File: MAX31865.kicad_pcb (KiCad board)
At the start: 2 copper layers, 25.4 x 27.9 mm, 29 parts, among them U1 MAX31865, U3 MIC5225-3.3, X1 3.5mm, X2 3.5mm

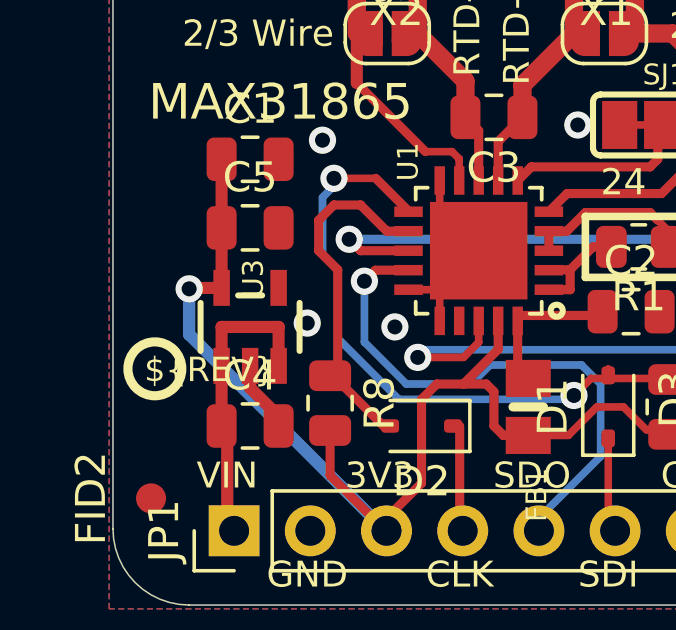
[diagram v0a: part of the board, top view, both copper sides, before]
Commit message: changed sot-23-5 footprint in schematic and pcb layout
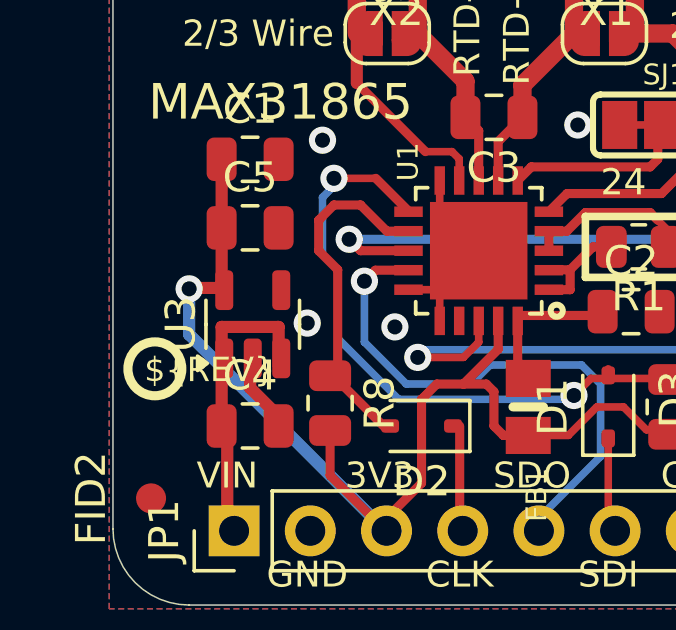
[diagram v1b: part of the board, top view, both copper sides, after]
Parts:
- U3: footprint SOT23-5 -> Package_TO_SOT_SMD:SOT-23-5
- moved U3 0.12 mm to (140.5, 109.6), turned to 90 degrees
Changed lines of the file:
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@@
 		)
 	)
-	(footprint "SOT23-5"
+	(footprint "Package_TO_SOT_SMD:SOT-23-5"
 		(layer "F.Cu")
-		(at 140.3731 109.7026)
-		(descr "Small Outline Transistor - 5 Pin")
+		(at 140.4606 109.6151 90)
+		(descr "SOT, 5 Pin (https://www.jedec.org/sites/default/files/docs/Mo-178c.PDF variant AA), generated with kicad-footprint-generator ipc_gullwing_generator.py")
+		(tags "SOT TO_SOT_SMD")
 		(property "Reference" "U3"
-			(at 0.508 -0.962 90)
+			(at 0 -2.4 270)
+			(layer "F.SilkS")
+			(effects
+				(font
+					(size 1 1)
+					(thickness 0.15)
+				)
+			)
+		)
+		(property "Value" "MIC5225-3.3"
+			(at 0 2.4 270)
+			(layer "F.Fab")
+			(effects
+				(font
+					(size 1 1)
+					(thickness 0.15)
+				)
+			)
+		)
+		(property "Footprint" ""
+			(at 0 0 90)
 			(unlocked yes)
-			(layer "F.SilkS")
-			(effects
-				(font
-					(size 0.692831 0.692831)
-					(thickness 0.119969)
-				)
-				(justify left bottom)
-			)
-		)
-		(property "Value" "MIC5225-3.3"
-			(at -4.899 -0.762 0)
+			(layer "F.Fab")
+			(hide yes)
+			(effects
+				(font
+					(size 1.27 1.27)
+				)
+			)
+		)
+		(property "Datasheet" ""
+			(at 0 0 90)
 			(unlocked yes)
 			(layer "F.Fab")
-			(effects
-				(font
-					(size 0.979424 0.979424)
-					(thickness 0.036576)
-				)
-				(justify right top)
-			)
-		)
-		(property "Footprint" ""
-			(at 0 0 0)
+			(hide yes)
+			(effects
+				(font
+					(size 1.27 1.27)
+				)
+			)
+		)
+		(property "Description" ""
+			(at 0 0 90)
 			(unlocked yes)
 			(layer "F.Fab")
@@
 			)
 		)
-		(property "Datasheet" ""
-			(at 0 0 0)
-			(unlocked yes)
-			(layer "F.Fab")
-			(hide yes)
-			(effects
-				(font
-					(size 1.27 1.27)
-				)
-			)
-		)
-		(property "Description" ""
-			(at 0 0 0)
-			(unlocked yes)
-			(layer "F.Fab")
-			(hide yes)
-			(effects
-				(font
-					(size 1.27 1.27)
-				)
-			)
-		)
-		(fp_line
-			(start -1.65 -0.8)
-			(end -1.65 0.8)
-			(stroke
-				(width 0.2032)
-				(type solid)
-			)
-			(layer "F.SilkS")
-		)
-		(fp_line
-			(start -0.4 -1.05)
-			(end 0.4 -1.05)
-			(stroke
-				(width 0.2032)
-				(type solid)
-			)
-			(layer "F.SilkS")
-		)
-		(fp_line
-			(start 1.65 -0.8)
-			(end 1.65 0.8)
-			(stroke
-				(width 0.2032)
-				(type solid)
-			)
-			(layer "F.SilkS")
-		)
-		(fp_line
-			(start -1.4224 -0.8104)
-			(end 1.4224 -0.8104)
-			(stroke
-				(width 0.2032)
-				(type solid)
-			)
-			(layer "F.Fab")
-		)
-		(fp_line
-			(start -1.4224 0.8104)
-			(end -1.4224 -0.8104)
-			(stroke
-				(width 0.2032)
-				(type solid)
-			)
-			(layer "F.Fab")
-		)
-		(fp_line
-			(start 1.4224 -0.8104)
-			(end 1.4224 0.8104)
-			(stroke
-				(width 0.2032)
-				(type solid)
-			)
-			(layer "F.Fab")
-		)
-		(fp_line
-			(start 1.4224 0.8104)
-			(end -1.4224 0.8104)
-			(stroke
-				(width 0.2032)
-				(type solid)
-			)
-			(layer "F.Fab")
+		(attr smd)
+		(fp_line
+			(start 0 -1.56)
+			(end 0.8 -1.56)
+			(stroke
+				(width 0.12)
+				(type solid)
+			)
+			(layer "F.SilkS")
+		)
+		(fp_line
+			(start 0 -1.56)
+			(end -0.8 -1.56)
+			(stroke
+				(width 0.12)
+				(type solid)
+			)
+			(layer "F.SilkS")
+		)
+		(fp_line
+			(start 0 1.56)
+			(end 0.8 1.56)
+			(stroke
+				(width 0.12)
+				(type solid)
+			)
+			(layer "F.SilkS")
+		)
+		(fp_line
+			(start 0 1.56)
+			(end -0.8 1.56)
+			(stroke
+				(width 0.12)
+				(type solid)
+			)
+			(layer "F.SilkS")
 		)
 		(fp_poly
 			(pts
-				(xy -1.2 -0.85) (xy -0.7 -0.85) (xy -0.7 -1.5) (xy -1.2 -1.5)
-			)
-			(stroke
-				(width 0)
-				(type default)
+				(xy -1.3 -1.51) (xy -1.54 -1.84) (xy -1.06 -1.84) (xy -1.3 -1.51)
+			)
+			(stroke
+				(width 0.12)
+				(type solid)
 			)
 			(fill solid)
-			(layer "F.Fab")
-		)
-		(fp_poly
-			(pts
-				(xy -1.2 1.5) (xy -0.7 1.5) (xy -0.7 0.85) (xy -1.2 0.85)
-			)
-			(stroke
-				(width 0)
-				(type default)
-			)
-			(fill solid)
-			(layer "F.Fab")
-		)
-		(fp_poly
-			(pts
-				(xy -0.25 1.5) (xy 0.25 1.5) (xy 0.25 0.85) (xy -0.25 0.85)
-			)
-			(stroke
-				(width 0)
-				(type default)
-			)
-			(fill solid)
-			(layer "F.Fab")
-		)
-		(fp_poly
-			(pts
-				(xy 0.7 -0.85) (xy 1.2 -0.85) (xy 1.2 -1.5) (xy 0.7 -1.5)
-			)
-			(stroke
-				(width 0)
-				(type default)
-			)
-			(fill solid)
-			(layer "F.Fab")
-		)
-		(fp_poly
-			(pts
-				(xy 0.7 1.5) (xy 1.2 1.5) (xy 1.2 0.85) (xy 0.7 0.85)
-			)
-			(stroke
-				(width 0)
-				(type default)
-			)
-			(fill solid)
-			(layer "F.Fab")
-		)
-		(pad "1" smd rect
-			(at -0.95 1.3001)
-			(size 0.55 1.2)
-			(layers "F.Cu" "F.Paste" "F.Mask")
+			(layer "F.SilkS")
+		)
+		(fp_line
+			(start 2.05 -1.7)
+			(end -2.05 -1.7)
+			(stroke
+				(width 0.05)
+				(type solid)
+			)
+			(layer "F.CrtYd")
+		)
+		(fp_line
+			(start -2.05 -1.7)
+			(end -2.05 1.7)
+			(stroke
+				(width 0.05)
+				(type solid)
+			)
+			(layer "F.CrtYd")
+		)
+		(fp_line
+			(start 2.05 1.7)
+			(end 2.05 -1.7)
+			(stroke
+				(width 0.05)
+				(type solid)
+			)
+			(layer "F.CrtYd")
+		)
+		(fp_line
+			(start -2.05 1.7)
+			(end 2.05 1.7)
+			(stroke
+				(width 0.05)
+				(type solid)
+			)
+			(layer "F.CrtYd")
+		)
+		(fp_line
+			(start 0.8 -1.45)
+			(end 0.8 1.45)
+			(stroke
+				(width 0.1)
+				(type solid)
+			)
+			(layer "F.Fab")
+		)
+		(fp_line
+			(start -0.4 -1.45)
+			(end 0.8 -1.45)
+			(stroke
+				(width 0.1)
+				(type solid)
+			)
+			(layer "F.Fab")
+		)
+		(fp_line
+			(start -0.8 -1.05)
+			(end -0.4 -1.45)
+			(stroke
+				(width 0.1)
+				(type solid)
+			)
+			(layer "F.Fab")
+		)
+		(fp_line
+			(start 0.8 1.45)
+			(end -0.8 1.45)
+			(stroke
+				(width 0.1)
+				(type solid)
+			)
+			(layer "F.Fab")
+		)
+		(fp_line
+			(start -0.8 1.45)
+			(end -0.8 -1.05)
+			(stroke
+				(width 0.1)
+				(type solid)
+			)
+			(layer "F.Fab")
+		)
+		(fp_text user "${REFERENCE}"
+			(at 0 0 270)
+			(layer "F.Fab")
+			(effects
+				(font
+					(size 0.4 0.4)
+					(thickness 0.06)
+				)
+			)
+		)
+		(pad "1" smd roundrect
+			(at -1.1375 -0.95 90)
+			(size 1.325 0.6)
+			(layers "F.Cu" "F.Paste" "F.Mask")
+			(roundrect_rratio 0.25)
 			(net 18 "VIN")
-			(solder_mask_margin 0.0508)
-			(thermal_bridge_angle 0)
-		)
-		(pad "2" smd rect
-			(at 0 1.3001)
-			(size 0.55 1.2)
-			(layers "F.Cu" "F.Paste" "F.Mask")
+		)
+		(pad "2" smd roundrect
+			(at -1.1375 0 90)
+			(size 1.325 0.6)
+			(layers "F.Cu" "F.Paste" "F.Mask")
+			(roundrect_rratio 0.25)
 			(net 1 "GND")
-			(solder_mask_margin 0.0508)
-			(thermal_bridge_angle 0)
-		)
-		(pad "3" smd rect
-			(at 0.95 1.3001)
-			(size 0.55 1.2)
-			(layers "F.Cu" "F.Paste" "F.Mask")
+		)
+		(pad "3" smd roundrect
+			(at -1.1375 0.95 90)
+			(size 1.325 0.6)
+			(layers "F.Cu" "F.Paste" "F.Mask")
+			(roundrect_rratio 0.25)
 			(net 18 "VIN")
-			(solder_mask_margin 0.0508)
-			(thermal_bridge_angle 0)
-		)
-		(pad "4" smd rect
-			(at 0.95 -1.3001)
-			(size 0.55 1.2)
-			(layers "F.Cu" "F.Paste" "F.Mask")
-			(solder_mask_margin 0.0508)
-			(thermal_bridge_angle 0)
-		)
-		(pad "5" smd rect
-			(at -0.95 -1.3001)
-			(size 0.55 1.2)
-			(layers "F.Cu" "F.Paste" "F.Mask")
+		)
+		(pad "4" smd roundrect
+			(at 1.1375 0.95 90)
+			(size 1.325 0.6)
+			(layers "F.Cu" "F.Paste" "F.Mask")
+			(roundrect_rratio 0.25)
+		)
+		(pad "5" smd roundrect
+			(at 1.1375 -0.95 90)
+			(size 1.325 0.6)
+			(layers "F.Cu" "F.Paste" "F.Mask")
+			(roundrect_rratio 0.25)
 			(net 2 "VDD")
-			(solder_mask_margin 0.0508)
-			(thermal_bridge_angle 0)
+		)
+		(model "${KICAD8_3DMODEL_DIR}/Package_TO_SOT_SMD.3dshapes/SOT-23-5.wrl"
+			(offset
+				(xyz 0 0 0)
+			)
+			(scale
+				(xyz 1 1 1)
+			)
+			(rotate
+				(xyz 0 0 0)
+			)
 		)
 	)

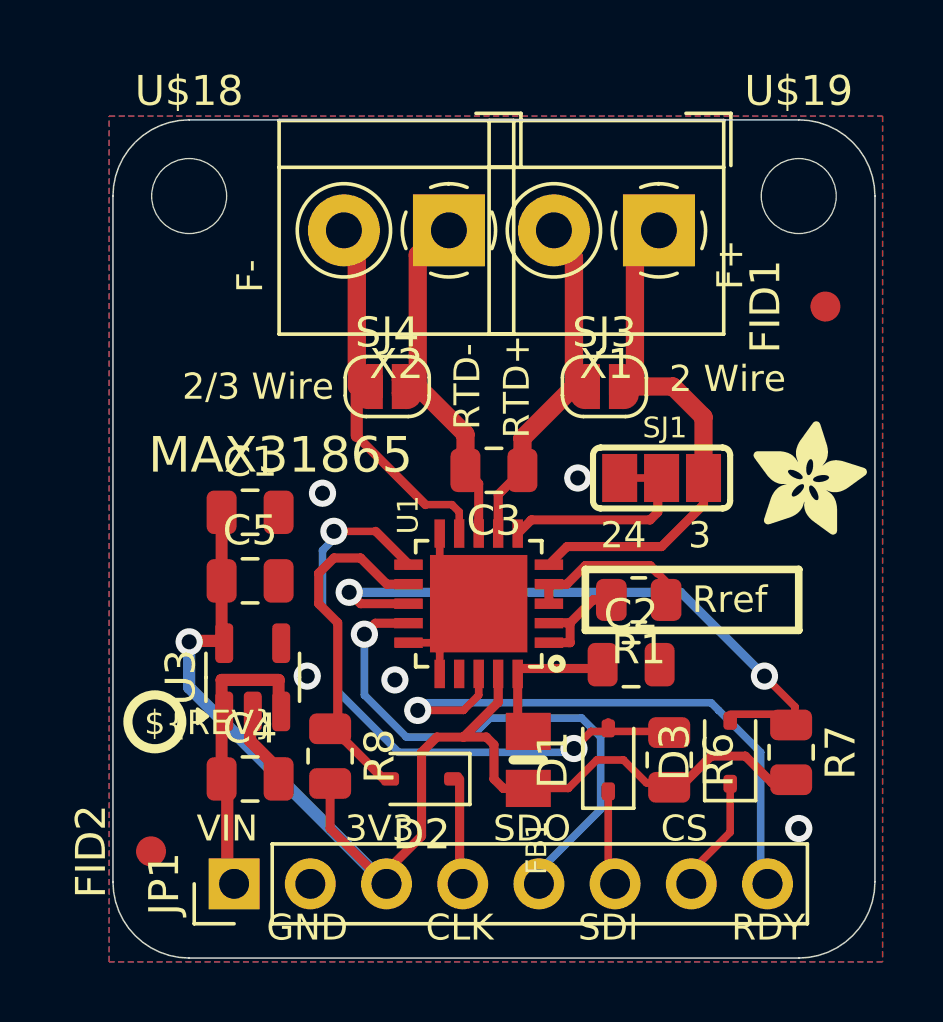
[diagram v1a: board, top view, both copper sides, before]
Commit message: changed 3 way solde jumper footprint in schematic and pcb layout
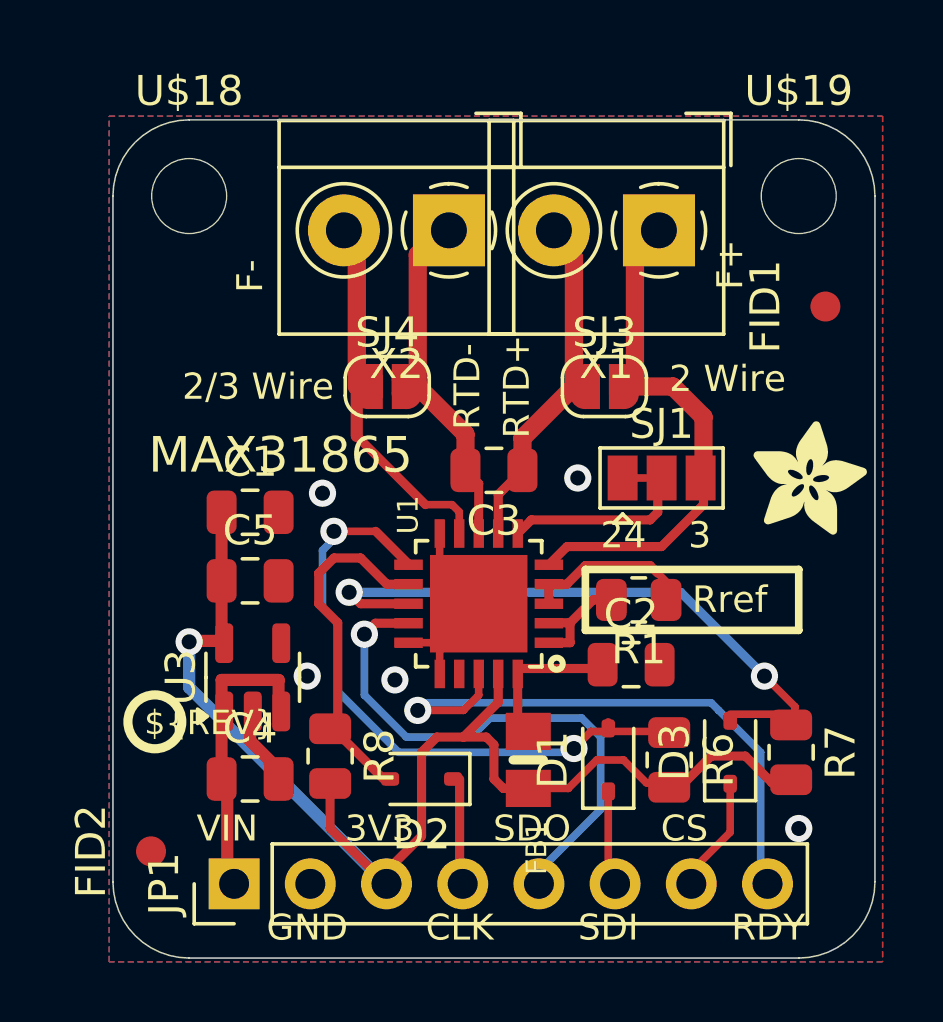
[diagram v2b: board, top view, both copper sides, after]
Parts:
- SJ1: footprint SOLDERJUMPER_2WAY_OPEN_NOPASTE -> Jumper:SolderJumper-3_P1.3mm_Open_Pad1.0x1.5mm
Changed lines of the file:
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@@
 		)
 	)
-	(footprint "SOLDERJUMPER_2WAY_OPEN_NOPASTE"
+	(footprint "Jumper:SolderJumper-3_P1.3mm_Open_Pad1.0x1.5mm"
 		(layer "F.Cu")
 		(at 154.0891 102.9716)
+		(descr "SMD Solder 3-pad Jumper, 1x1.5mm Pads, 0.3mm gap, open")
+		(tags "solder jumper open")
 		(property "Reference" "SJ1"
-			(at -0.635 -1.27 0)
-			(unlocked yes)
-			(layer "F.SilkS")
-			(effects
-				(font
-					(size 0.692831 0.692831)
-					(thickness 0.119969)
-				)
-				(justify left bottom)
+			(at 0 -1.8 0)
+			(layer "F.SilkS")
+			(effects
+				(font
+					(size 1 1)
+					(thickness 0.15)
+				)
 			)
 		)
 		(property "Value" ""
-			(at 1.0351 0 0)
-			(unlocked yes)
-			(layer "F.Fab")
-			(effects
-				(font
-					(size 0.0254 0.0254)
-					(thickness 0.002032)
-				)
-				(justify left bottom)
+			(at 0 2 0)
+			(layer "F.Fab")
+			(effects
+				(font
+					(size 1 1)
+					(thickness 0.15)
+				)
 			)
 		)
@@
 			)
 		)
-		(fp_line
-			(start -2.286 0.762)
-			(end -2.286 -0.762)
-			(stroke
-				(width 0.2032)
-				(type solid)
-			)
-			(layer "F.SilkS")
-		)
-		(fp_line
-			(start -2.032 -1.016)
-			(end 2.032 -1.016)
-			(stroke
-				(width 0.2032)
-				(type solid)
-			)
-			(layer "F.SilkS")
-		)
-		(fp_line
-			(start 2.032 1.016)
-			(end -2.032 1.016)
-			(stroke
-				(width 0.2032)
-				(type solid)
-			)
-			(layer "F.SilkS")
-		)
-		(fp_line
-			(start 2.286 0.762)
-			(end 2.286 -0.762)
-			(stroke
-				(width 0.2032)
-				(type solid)
-			)
-			(layer "F.SilkS")
-		)
-		(fp_arc
-			(start -2.286 -0.762)
-			(mid -2.211605 -0.941605)
-			(end -2.032 -1.016)
-			(stroke
-				(width 0.2032)
-				(type solid)
-			)
-			(layer "F.SilkS")
-		)
-		(fp_arc
-			(start -2.032 1.016)
-			(mid -2.211605 0.941605)
-			(end -2.286 0.762)
-			(stroke
-				(width 0.2032)
-				(type solid)
-			)
-			(layer "F.SilkS")
-		)
-		(fp_arc
-			(start 2.032 -1.016)
-			(mid 2.211605 -0.941605)
-			(end 2.286 -0.762)
-			(stroke
-				(width 0.2032)
-				(type solid)
-			)
-			(layer "F.SilkS")
-		)
-		(fp_arc
-			(start 2.286 0.762)
-			(mid 2.211605 0.941605)
-			(end 2.032 1.016)
-			(stroke
-				(width 0.2032)
-				(type solid)
-			)
-			(layer "F.SilkS")
-		)
-		(fp_poly
-			(pts
-				(xy -2.1 0.9) (xy 2.1 0.9) (xy 2.1 -0.9) (xy -2.1 -0.9)
-			)
-			(stroke
-				(width 0)
-				(type default)
-			)
-			(fill solid)
-			(layer "F.Mask")
-		)
-		(fp_line
-			(start -1.651 0)
-			(end -2.159 0)
-			(stroke
-				(width 0.2032)
-				(type solid)
-			)
-			(layer "F.Fab")
-		)
-		(fp_line
-			(start 1.651 0)
-			(end 2.159 0)
-			(stroke
-				(width 0.2032)
-				(type solid)
-			)
-			(layer "F.Fab")
-		)
-		(fp_arc
-			(start -0.889 0.127)
-			(mid -1.016 0)
-			(end -0.889 -0.127)
-			(stroke
-				(width 1.27)
-				(type solid)
-			)
-			(layer "F.Fab")
-		)
-		(fp_arc
-			(start 0.889 -0.127)
-			(mid 1.016 0)
-			(end 0.889 0.127)
-			(stroke
-				(width 1.27)
-				(type solid)
-			)
-			(layer "F.Fab")
-		)
-		(fp_poly
-			(pts
-				(xy -0.508 0.762) (xy 0.508 0.762) (xy 0.508 -0.762) (xy -0.508 -0.762)
-			)
-			(stroke
-				(width 0)
-				(type default)
-			)
-			(fill solid)
-			(layer "F.Fab")
+		(zone_connect 1)
+		(attr exclude_from_pos_files exclude_from_bom)
+		(fp_line
+			(start -2.05 -1)
+			(end 2.05 -1)
+			(stroke
+				(width 0.12)
+				(type solid)
+			)
+			(layer "F.SilkS")
+		)
+		(fp_line
+			(start -2.05 1)
+			(end -2.05 -1)
+			(stroke
+				(width 0.12)
+				(type solid)
+			)
+			(layer "F.SilkS")
+		)
+		(fp_line
+			(start -1.6 1.5)
+			(end -1 1.5)
+			(stroke
+				(width 0.12)
+				(type solid)
+			)
+			(layer "F.SilkS")
+		)
+		(fp_line
+			(start -1.3 1.2)
+			(end -1.6 1.5)
+			(stroke
+				(width 0.12)
+				(type solid)
+			)
+			(layer "F.SilkS")
+		)
+		(fp_line
+			(start -1.3 1.2)
+			(end -1 1.5)
+			(stroke
+				(width 0.12)
+				(type solid)
+			)
+			(layer "F.SilkS")
+		)
+		(fp_line
+			(start 2.05 -1)
+			(end 2.05 1)
+			(stroke
+				(width 0.12)
+				(type solid)
+			)
+			(layer "F.SilkS")
+		)
+		(fp_line
+			(start 2.05 1)
+			(end -2.05 1)
+			(stroke
+				(width 0.12)
+				(type solid)
+			)
+			(layer "F.SilkS")
+		)
+		(fp_line
+			(start -2.3 -1.25)
+			(end -2.3 1.25)
+			(stroke
+				(width 0.05)
+				(type solid)
+			)
+			(layer "F.CrtYd")
+		)
+		(fp_line
+			(start -2.3 -1.25)
+			(end 2.3 -1.25)
+			(stroke
+				(width 0.05)
+				(type solid)
+			)
+			(layer "F.CrtYd")
+		)
+		(fp_line
+			(start 2.3 1.25)
+			(end -2.3 1.25)
+			(stroke
+				(width 0.05)
+				(type solid)
+			)
+			(layer "F.CrtYd")
+		)
+		(fp_line
+			(start 2.3 1.25)
+			(end 2.3 -1.25)
+			(stroke
+				(width 0.05)
+				(type solid)
+			)
+			(layer "F.CrtYd")
 		)
 		(fp_text user "3"
@@
 		)
 		(pad "1" smd rect
-			(at -1.397 0)
-			(size 1.1684 1.6002)
-			(layers "F.Cu")
+			(at -1.3 0)
+			(size 1 1.5)
+			(layers "F.Cu" "F.Mask")
 			(net 1 "GND")
-			(solder_mask_margin 0.0508)
-			(thermal_bridge_angle 0)
 		)
 		(pad "2" smd rect
 			(at 0 0)
-			(size 1.1684 1.6002)
-			(layers "F.Cu")
+			(size 1 1.5)
+			(layers "F.Cu" "F.Mask")
 			(net 7 "N$11")
-			(solder_mask_margin 0.0508)
-			(thermal_bridge_angle 0)
 		)
 		(pad "3" smd rect
-			(at 1.397 0)
-			(size 1.1684 1.6002)
-			(layers "F.Cu")
+			(at 1.3 0)
+			(size 1 1.5)
+			(layers "F.Cu" "F.Mask")
 			(net 6 "FORCE+")
-			(solder_mask_margin 0.0508)
-			(thermal_bridge_angle 0)
 		)
 	)
